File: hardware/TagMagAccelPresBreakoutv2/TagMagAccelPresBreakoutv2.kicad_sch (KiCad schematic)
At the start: 34 parts, among them J1 Conn_01x06, J2 Conn_01x04, J3 Conn_01x04, J4 Conn_01x06, J401 CONN_01X02, J5 Conn_01x06, J6 Conn_02x04_Counter_Clockwise, Q501 Q_NPN_BEC, U1 at25xe321D-UUN, U2 LIS2DU12TR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

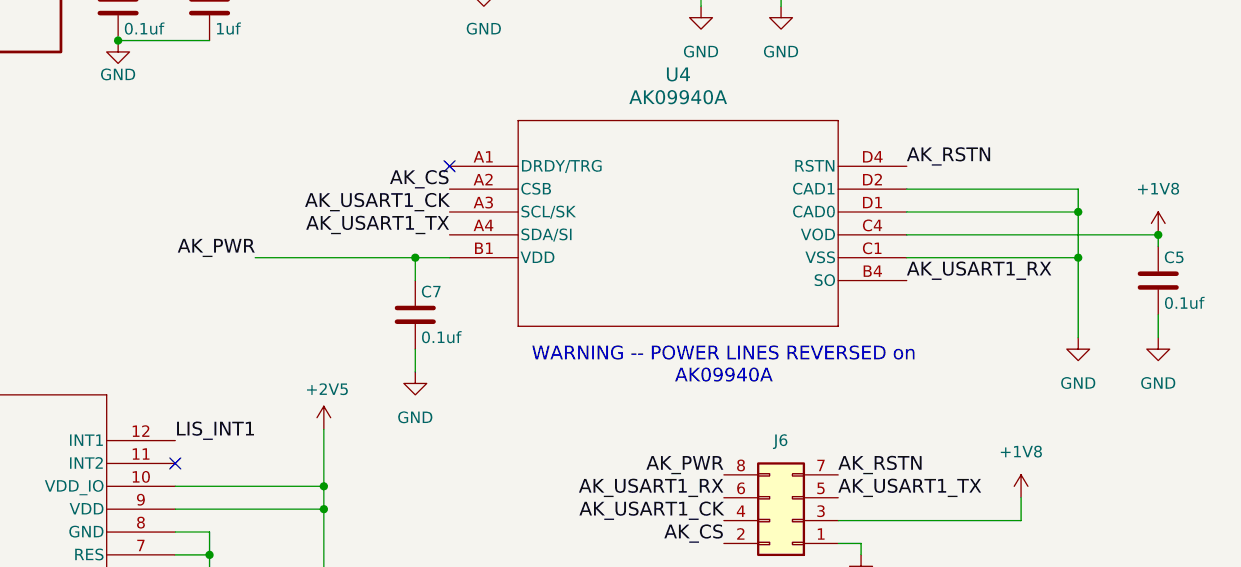
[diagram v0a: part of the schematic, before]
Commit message: designed compass tag
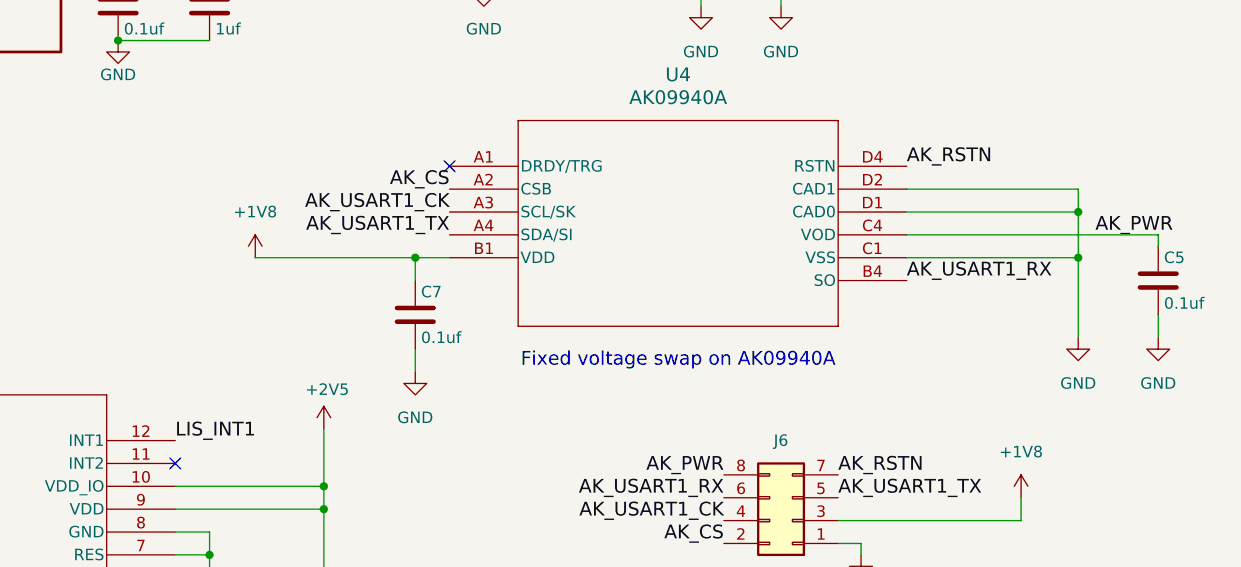
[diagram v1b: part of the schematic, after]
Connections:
- net +1V8: now also C7.1, U4.B1 (VDD); no longer C5.1, U4.C4 (VOD)
- net AK_PWR: now also C5.1, U4.C4 (VOD); no longer C7.1, U4.B1 (VDD)
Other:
- note added: "Fixed voltage swap on AK09940A"
- note removed: "WARNING -- POWER LINES REVERSED on AK09940A"
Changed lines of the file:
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@@
 	(title_block
 		(title "Tag with Mag, Accel,Pressure")
-		(date "2025-03-20")
+		(date "2025-04-16")
+		(rev "v2")
 		(company "IUCS")
 		(comment 1 "Geoffrey Brown")
@@
 	)
 	(junction
-		(at 259.08 109.22)
-		(diameter 0)
-		(color 0 0 0 0)
-	)
-	(junction
 		(at 46.99 118.11)
 		(diameter 0)
@@
 		)
 	)
-	(text "WARNING -- POWER LINES REVERSED on\nAK09940A"
+	(text "Note LPS_RX/LPS_TX swapped -- must be configured in software"
 		(exclude_from_sim no)
-		(at 210.82 123.825 0)
+		(at 162.306 16.256 0)
 		(effects
 			(font
 				(size 1.524 1.524)
-				(color 255 25 71 1)
 			)
 		)
 	)
-	(text "Note LPS_RX/LPS_TX swapped -- must be configured in software"
+	(text "Fixed voltage swap on AK09940A"
 		(exclude_from_sim no)
-		(at 162.306 16.256 0)
+		(at 205.74 123.19 0)
 		(effects
 			(font
@@
 	)
 	(label "AK_PWR"
-		(at 158.75 111.76 180)
+		(at 252.095 109.22 0)
 		(effects
 			(font
 				(size 1.524 1.524)
 			)
-			(justify right bottom)
+			(justify left bottom)
 		)
 	)
@@
 	(symbol
 		(lib_id "power:+1V8")
-		(at 259.08 109.22 0)
+		(at 158.75 111.76 0)
 		(unit 1)
 		(exclude_from_sim no)
@@
 		(fields_autoplaced yes)
 		(property "Reference" "#PWR17"
-			(at 259.08 113.03 0)
+			(at 158.75 115.57 0)
 			(effects
 				(font
@@
 		)
 		(property "Value" "+1V8"
-			(at 259.08 104.14 0)
+			(at 158.75 106.68 0)
 			(effects
 				(font
@@
 		)
 		(property "Footprint" ""
-			(at 259.08 109.22 0)
+			(at 158.75 111.76 0)
 			(effects
 				(font
@@
 		)
 		(property "Datasheet" ""
-			(at 259.08 109.22 0)
+			(at 158.75 111.76 0)
 			(effects
 				(font
@@
 		)
 		(property "Description" "Power symbol creates a global label with name \"+1V8\""
-			(at 259.08 109.22 0)
+			(at 158.75 111.76 0)
 			(effects
 				(font
